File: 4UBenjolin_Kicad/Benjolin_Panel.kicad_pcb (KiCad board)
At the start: 2 copper layers, 108 x 177.8 mm, 17 parts

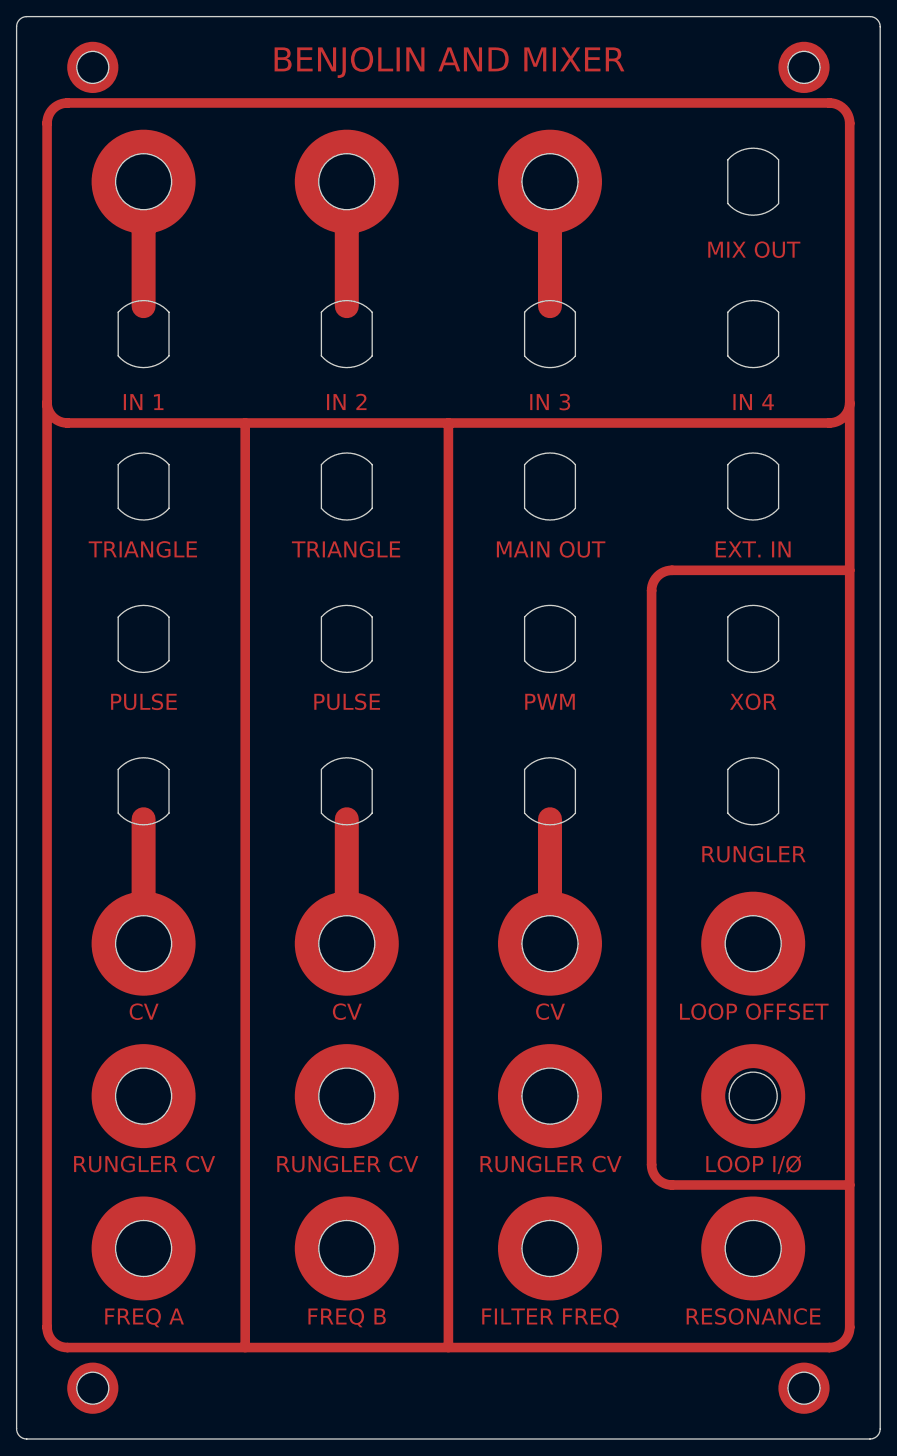
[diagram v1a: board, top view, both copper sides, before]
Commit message: Changed to circular holes on the front panel
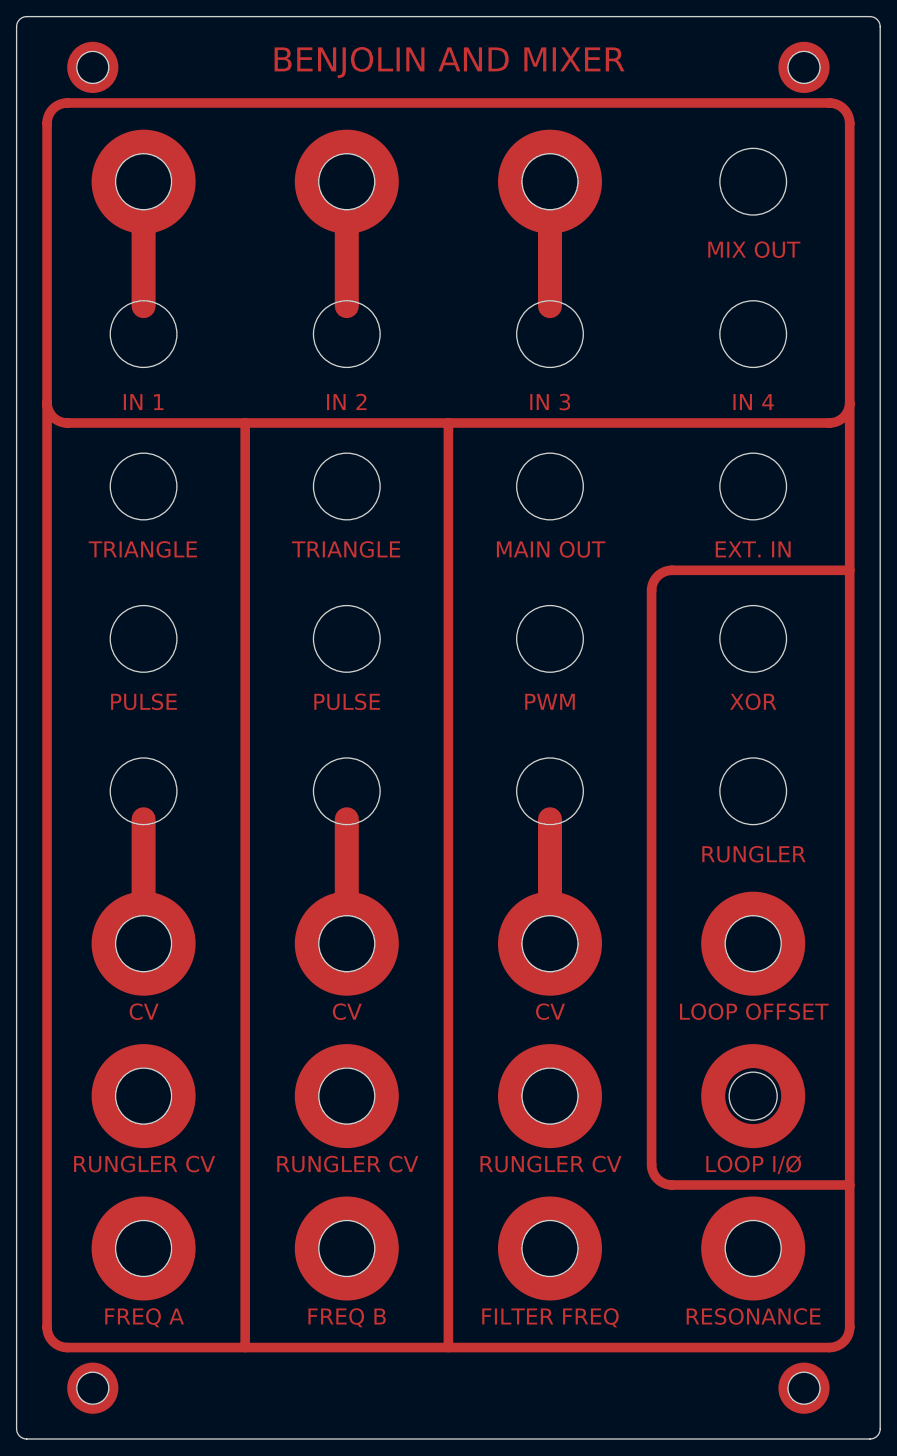
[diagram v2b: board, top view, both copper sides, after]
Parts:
- REF** (x17): footprint SynthComponents:Banana _Jack_Panel -> SynthComponents:Banana _Jack_Panel_Round
